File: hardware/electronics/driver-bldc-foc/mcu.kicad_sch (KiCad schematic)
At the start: 1 part, among them U2 STM32G473RETx

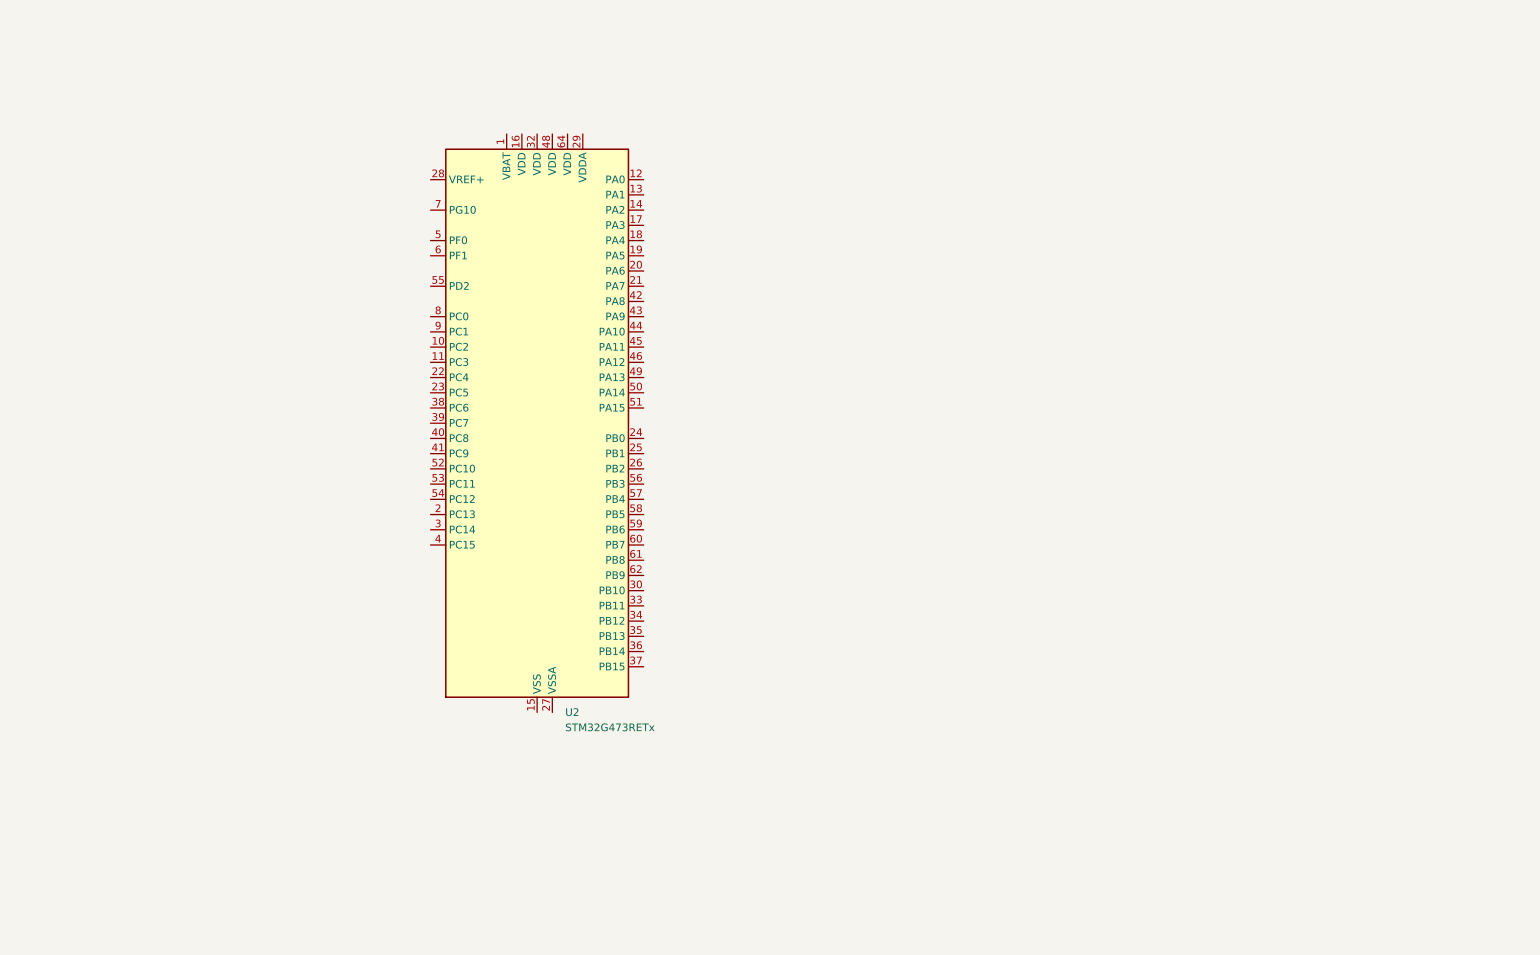
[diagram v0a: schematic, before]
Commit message: update mcu schematic
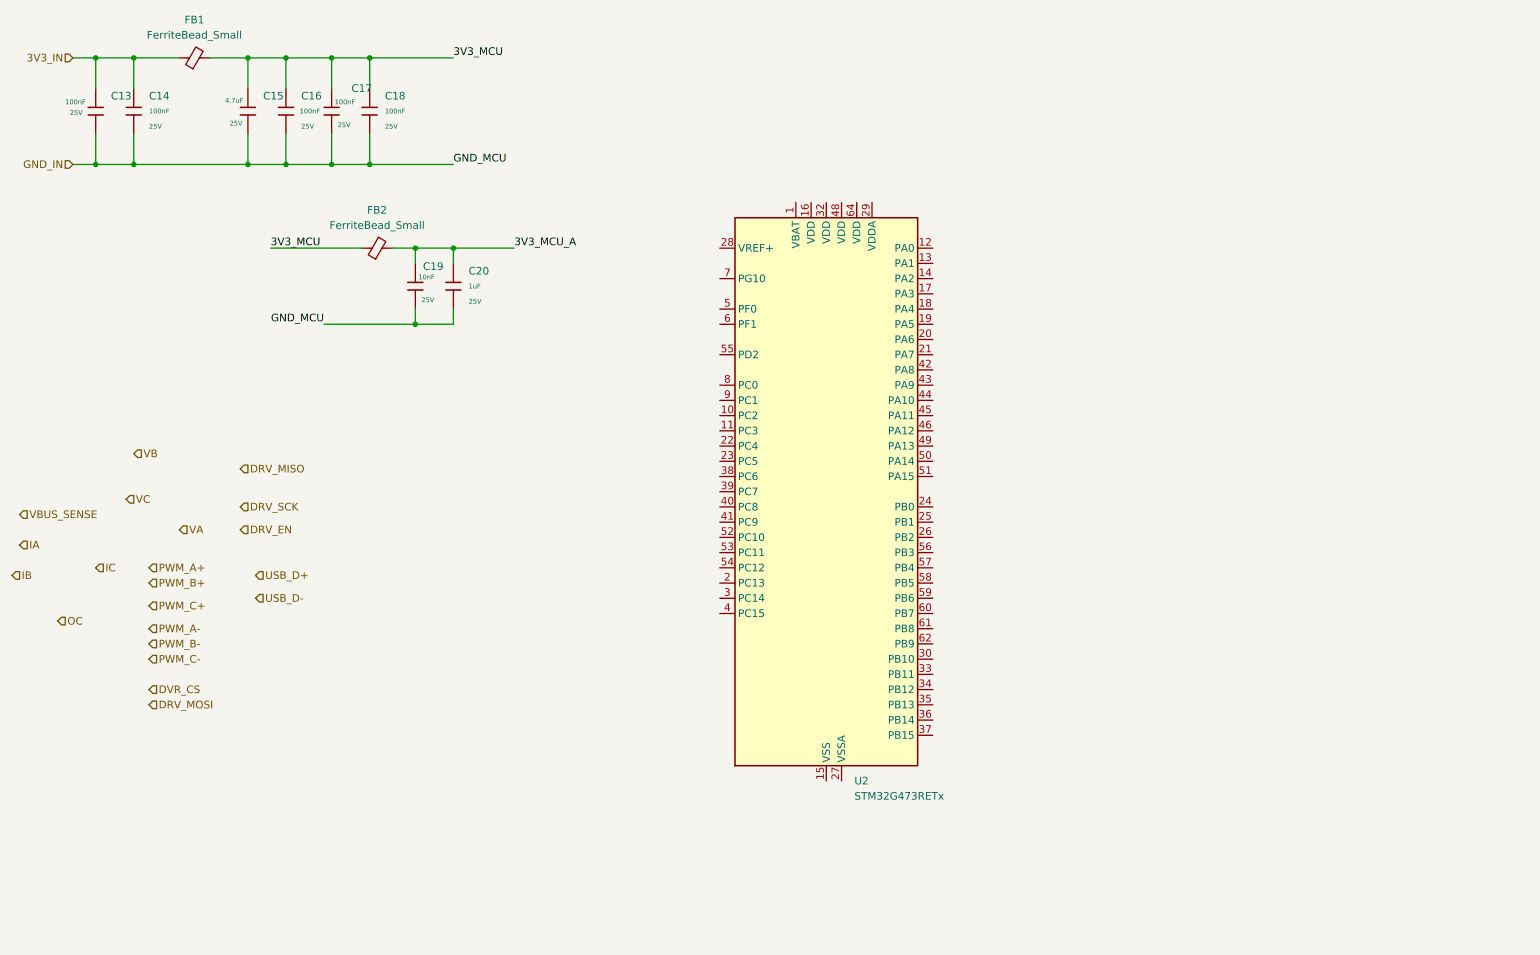
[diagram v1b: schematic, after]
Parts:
- added C13, C14, C16, C17, C18: 100nF, Capacitor_SMD:C_0805_2012Metric, symbol JLCPCB-Capacitors:0805,10uF
- added C15: 4.7uF, Capacitor_SMD:C_0805_2012Metric, symbol JLCPCB-Capacitors:0805,10uF
- added C19: 10nF, Capacitor_SMD:C_0805_2012Metric, symbol JLCPCB-Capacitors:0805,10uF
- added C20: 1uF, Capacitor_SMD:C_0805_2012Metric, symbol JLCPCB-Capacitors:0805,10uF
- added FB1, FB2: FerriteBead_Small, Inductor_SMD:L_0201_0603Metric, symbol Device:FerriteBead_Small
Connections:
- new net 3V3_IN: C13.1, C14.1, FB1.1
- new net 3V3_MCU: C15.1, C16.1, C17.1, C18.1, FB1.2, FB2.1
- new net 3V3_MCU_A: C19.1, C20.1, FB2.2
- new net GND_IN: C13.2, C14.2, C15.2, C16.2, C17.2, C18.2, C19.2, C20.2
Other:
- moved on the sheet: U2

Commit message: update mcu schematic
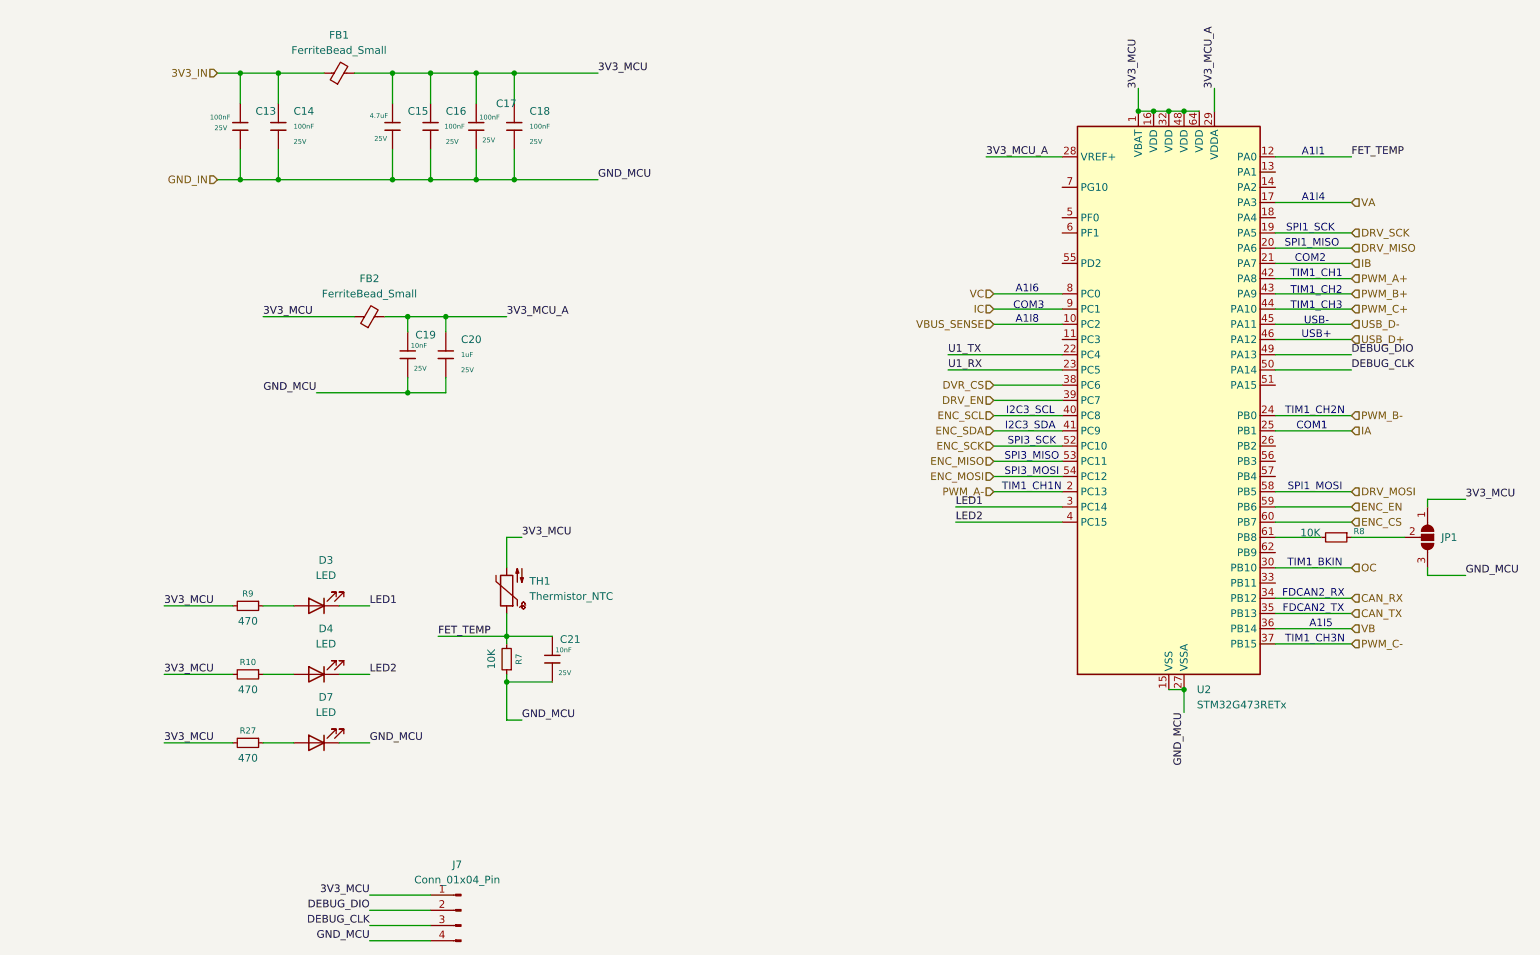
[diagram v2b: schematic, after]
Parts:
- added C21: 10nF, Capacitor_SMD:C_0805_2012Metric, symbol JLCPCB-Capacitors:0805,10uF
- added D3, D4, D7: LED, LED_SMD:LED_0805_2012Metric, symbol Device:LED
- added J7: Conn_01x04_Pin, Connector_JST:JST_XH_B4B-XH-A_1x04_P2.50mm_Vertical, symbol Connector:Conn_01x04_Pin
- added JP1: SolderJumper_3_Open, Jumper:SolderJumper-3_P1.3mm_Open_RoundedPad1.0x1.5mm_NumberLabels, symbol Jumper:SolderJumper_3_Open
- added R10, R27, R9: 470, Resistor_SMD:R_0805_2012Metric, symbol Device:R_Small
- added R7, R8: 10K, Resistor_SMD:R_0805_2012Metric, symbol Device:R_Small
- added TH1: Thermistor_NTC, Resistor_THT:R_Axial_DIN0204_L3.6mm_D1.6mm_P1.90mm_Vertical, symbol Device:Thermistor_NTC
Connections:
- net 3V3_MCU: now also U2.1 (VBAT), U2.16 (VDD), U2.32 (VDD), U2.48 (VDD), U2.64 (VDD), J7.1 (Pin_1), JP1.1 (A), R10.2, R27.2, R9.2, TH1.2
- net 3V3_MCU_A: now also U2.28 (VREF+), U2.29 (VDDA)
- net DRV_EN: now also U2.39 (PC7)
- net DRV_MISO: now also U2.20 (PA6)
- net DRV_MOSI: now also U2.58 (PB5)
- net DRV_SCK: now also U2.19 (PA5)
- net DVR_CS: now also U2.38 (PC6)
- net GND_IN: now also U2.15 (VSS), U2.27 (VSSA), U2.31 (VSS), U2.47 (VSS), U2.63 (VSS), C21.2, D7.1 (K), J7.4 (Pin_4), JP1.3 (B), R7.1
- net IA: now also U2.25 (PB1)
- net IB: now also U2.21 (PA7)
- net IC: now also U2.9 (PC1)
- net OC: now also U2.30 (PB10)
- net PWM_A+: now also U2.42 (PA8)
- net PWM_A-: now also U2.2 (PC13)
- net PWM_B+: now also U2.43 (PA9)
- net PWM_B-: now also U2.24 (PB0)
- net PWM_C+: now also U2.44 (PA10)
- net PWM_C-: now also U2.37 (PB15)
- net USB_D+: now also U2.46 (PA12)
- net USB_D-: now also U2.45 (PA11)
- net VA: now also U2.17 (PA3)
- net VB: now also U2.36 (PB14)
- net VBUS_SENSE: now also U2.10 (PC2)
- net VC: now also U2.8 (PC0)
- net FET_TEMP: now reaches U2.12 (PA0)
- net FET_TEMP: now also C21.1, R7.2, TH1.1
- net U1_TX: now reaches U2.22 (PC4)
- net U1_RX: now reaches U2.23 (PC5)
- net LED1: now reaches U2.3 (PC14)
- net LED1: now also D3.1 (K)
- net CAN_RX: now reaches U2.34 (PB12)
- net CAN_TX: now reaches U2.35 (PB13)
- net LED2: now reaches U2.4 (PC15)
- net LED2: now also D4.1 (K)
- net ENC_SCL: now reaches U2.40 (PC8)
- net ENC_SDA: now reaches U2.41 (PC9)
- net DEBUG_DIO: now reaches U2.49 (PA13)
- net DEBUG_DIO: now also J7.2 (Pin_2)
- net DEBUG_CLK: now reaches U2.50 (PA14)
- net DEBUG_CLK: now also J7.3 (Pin_3)
- net ENC_SCK: now reaches U2.52 (PC10)
- net ENC_MISO: now reaches U2.53 (PC11)
- net ENC_MOSI: now reaches U2.54 (PC12)
- net ENC_EN: now reaches U2.59 (PB6)
- net ENC_CS: now reaches U2.60 (PB7)
- net at U2.61 (PB8): now also R8.2
- new net: D4.2 (A), R10.1
- new net: JP1.2 (C), R8.1
- new net: D7.2 (A), R27.1
- new net: D3.2 (A), R9.1
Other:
- note added: "A1I1"
- note added: "A1I4"
- note added: "A1I5"
- note added: "A1I6"
- note added: "A1I8"
- note added: "COM1"
- note added: "COM2"
- note added: "COM3"
- note added: "FDCAN2_RX"
- note added: "FDCAN2_TX"
- note added: "I2C3_SCL"
- note added: "I2C3_SDA"
- note added: "SPI1_MISO"
- note added: "SPI1_MOSI"
- note added: "SPI1_SCK"
- note added: "SPI3_MISO"
- note added: "SPI3_MOSI"
- note added: "SPI3_SCK"
- note added: "TIM1_BKIN"
- note added: "TIM1_CH1"
- note added: "TIM1_CH1N"
- note added: "TIM1_CH2"
- note added: "TIM1_CH2N"
- note added: "TIM1_CH3"
- note added: "TIM1_CH3N"
- note added: "USB+"
- note added: "USB-"
- moved on the sheet: C13, C14, C15, C16, C17, C18, C19, C20, FB1, FB2, U2

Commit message: fix pcb
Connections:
- net DVR_CS renamed DRV_CS
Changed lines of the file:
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@@
 		)
 	)
-	(hierarchical_label "DVR_CS"
+	(hierarchical_label "DRV_CS"
 		(shape input)
 		(at 181.61 82.55 180)
